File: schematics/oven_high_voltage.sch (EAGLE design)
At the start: 6 parts, among them M1 Convection Fan

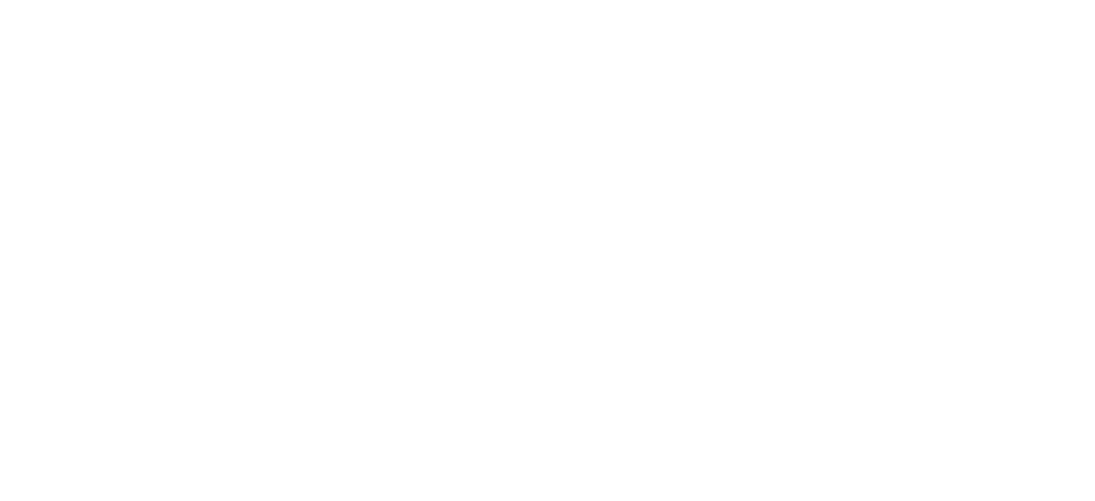
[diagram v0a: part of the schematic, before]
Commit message: Add custom title block.
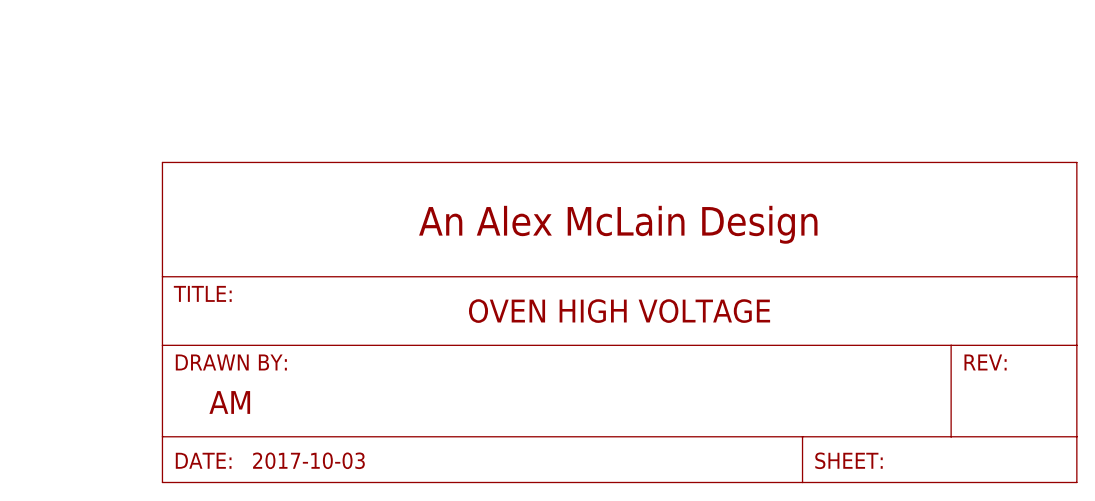
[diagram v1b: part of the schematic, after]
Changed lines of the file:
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@@
 <part name="M1" library="SparkFun-Electromechanical" deviceset="MOTOR" device="10MM" value="Convection Fan"/>
 <part name="GND1" library="SparkFun-PowerSymbols" deviceset="GND2" device="" value="Chassis Ground"/>
+<part name="FRAME1" library="frames" deviceset="LETTER_L" device="">
+<attribute name="COMPANY_NAME" value="An Alex McLain Design"/>
+<attribute name="DATE_DRAWN" value="2017-10-03"/>
+<attribute name="DRAWN_BY" value="AM"/>
+<attribute name="REV" value=""/>
+<attribute name="SHEET_NUM" value=""/>
+<attribute name="TITLE" value="OVEN HIGH VOLTAGE"/>
+</part>
 </parts>
 <sheets>
@@
 <attribute name="VALUE" x="101.6" y="77.724" size="1.778" layer="96" align="top-center"/>
 </instance>
+<instance part="FRAME1" gate="G$1" x="0" y="0">
+<attribute name="COMPANY_NAME" x="0" y="0" size="1.778" layer="96" display="off"/>
+<attribute name="DATE_DRAWN" x="0" y="0" size="1.778" layer="96" display="off"/>
+<attribute name="DRAWN_BY" x="0" y="0" size="1.778" layer="96" display="off"/>
+<attribute name="REV" x="0" y="0" size="1.778" layer="96" display="off"/>
+<attribute name="SHEET_NUM" x="0" y="0" size="1.778" layer="96" display="off"/>
+<attribute name="TITLE" x="0" y="0" size="1.778" layer="96" display="off"/>
+</instance>
+<instance part="FRAME1" gate="G$2" x="147.32" y="0"/>
 </instances>
 <busses>

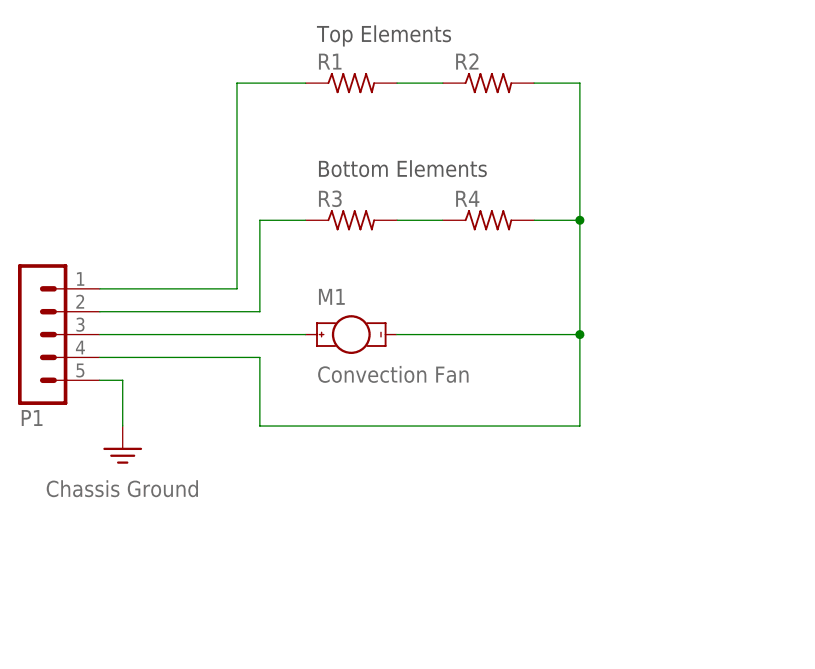
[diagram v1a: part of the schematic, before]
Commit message: Add controller relays schematic.
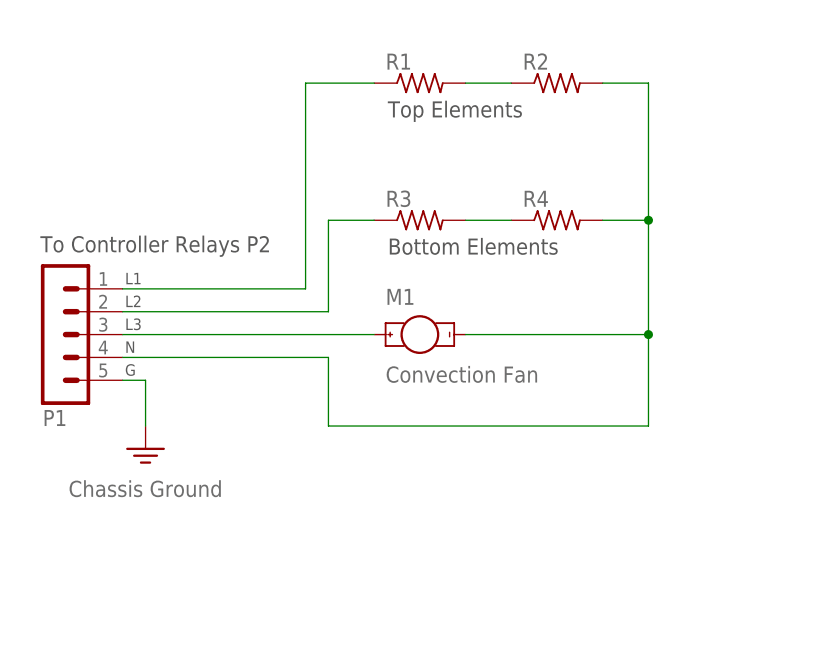
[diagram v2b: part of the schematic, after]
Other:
- note added: "G"
- note added: "L1"
- note added: "L2"
- note added: "L3"
- note added: "N"
- note added: "To Controller Relays P2"
- moved on the sheet: M1, P1, R1, R2, R3, R4
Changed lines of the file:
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@@
 <sheet>
 <plain>
-<text x="123.19" y="126.492" size="1.778" layer="97">Top Elements</text>
-<text x="123.19" y="111.506" size="1.778" layer="97">Bottom Elements</text>
+<text x="131.064" y="118.11" size="1.778" layer="97">Top Elements</text>
+<text x="101.854" y="99.568" size="1.27" layer="97">L1</text>
+<text x="101.854" y="97.028" size="1.27" layer="97">L2</text>
+<text x="101.854" y="94.488" size="1.27" layer="97">L3</text>
+<text x="101.854" y="91.948" size="1.27" layer="97">N</text>
+<text x="101.854" y="89.408" size="1.27" layer="97">G</text>
+<text x="92.456" y="103.124" size="1.778" layer="97">To Controller Relays P2</text>
+<text x="131.064" y="102.87" size="1.778" layer="97">Bottom Elements</text>
 </plain>
 <instances>
-<instance part="R1" gate="G$1" x="127" y="121.92"/>
-<instance part="R2" gate="G$1" x="142.24" y="121.92"/>
-<instance part="R3" gate="G$1" x="127" y="106.68"/>
-<instance part="R4" gate="G$1" x="142.24" y="106.68"/>
-<instance part="P1" gate="G$1" x="91.44" y="93.98" rot="MR180"/>
-<instance part="M1" gate="G$1" x="127" y="93.98" smashed="yes" rot="R90">
-<attribute name="NAME" x="123.19" y="97.282" size="1.778" layer="95" font="vector"/>
-<attribute name="VALUE" x="123.19" y="88.646" size="1.778" layer="96" font="vector"/>
+<instance part="R1" gate="G$1" x="134.62" y="121.92"/>
+<instance part="R2" gate="G$1" x="149.86" y="121.92"/>
+<instance part="R3" gate="G$1" x="134.62" y="106.68"/>
+<instance part="R4" gate="G$1" x="149.86" y="106.68"/>
+<instance part="P1" gate="G$1" x="93.98" y="93.98" rot="MR180"/>
+<instance part="M1" gate="G$1" x="134.62" y="93.98" smashed="yes" rot="R90">
+<attribute name="NAME" x="130.81" y="97.282" size="1.778" layer="95" font="vector"/>
+<attribute name="VALUE" x="130.81" y="88.646" size="1.778" layer="96" font="vector"/>
 </instance>
-<instance part="GND1" gate="G$1" x="101.6" y="81.28" smashed="yes">
-<attribute name="VALUE" x="101.6" y="77.724" size="1.778" layer="96" align="top-center"/>
+<instance part="GND1" gate="G$1" x="104.14" y="81.28" smashed="yes">
+<attribute name="VALUE" x="104.14" y="77.724" size="1.778" layer="96" align="top-center"/>
 </instance>
 <instance part="FRAME1" gate="G$1" x="0" y="0">
@@
 <pinref part="R1" gate="G$1" pin="2"/>
 <pinref part="R2" gate="G$1" pin="1"/>
-<wire x1="132.08" y1="121.92" x2="137.16" y2="121.92" width="0.1524" layer="91"/>
+<wire x1="139.7" y1="121.92" x2="144.78" y2="121.92" width="0.1524" layer="91"/>
 </segment>
 </net>
@@
 <pinref part="R3" gate="G$1" pin="2"/>
 <pinref part="R4" gate="G$1" pin="1"/>
-<wire x1="132.08" y1="106.68" x2="137.16" y2="106.68" width="0.1524" layer="91"/>
+<wire x1="139.7" y1="106.68" x2="144.78" y2="106.68" width="0.1524" layer="91"/>
 </segment>
 </net>
@@
 <pinref part="P1" gate="G$1" pin="3"/>
 <pinref part="M1" gate="G$1" pin="+"/>
-<wire x1="99.06" y1="93.98" x2="121.92" y2="93.98" width="0.1524" layer="91"/>
+<wire x1="101.6" y1="93.98" x2="129.54" y2="93.98" width="0.1524" layer="91"/>
 </segment>
 </net>
@@
 <segment>
 <pinref part="P1" gate="G$1" pin="2"/>
-<wire x1="99.06" y1="96.52" x2="116.84" y2="96.52" width="0.1524" layer="91"/>
-<wire x1="116.84" y1="96.52" x2="116.84" y2="106.68" width="0.1524" layer="91"/>
+<wire x1="101.6" y1="96.52" x2="124.46" y2="96.52" width="0.1524" layer="91"/>
+<wire x1="124.46" y1="96.52" x2="124.46" y2="106.68" width="0.1524" layer="91"/>
 <pinref part="R3" gate="G$1" pin="1"/>
-<wire x1="116.84" y1="106.68" x2="121.92" y2="106.68" width="0.1524" layer="91"/>
+<wire x1="124.46" y1="106.68" x2="129.54" y2="106.68" width="0.1524" layer="91"/>
 </segment>
 </net>
@@
 <segment>
 <pinref part="P1" gate="G$1" pin="1"/>
-<wire x1="99.06" y1="99.06" x2="114.3" y2="99.06" width="0.1524" layer="91"/>
-<wire x1="114.3" y1="99.06" x2="114.3" y2="121.92" width="0.1524" layer="91"/>
+<wire x1="101.6" y1="99.06" x2="121.92" y2="99.06" width="0.1524" layer="91"/>
+<wire x1="121.92" y1="99.06" x2="121.92" y2="121.92" width="0.1524" layer="91"/>
 <pinref part="R1" gate="G$1" pin="1"/>
-<wire x1="114.3" y1="121.92" x2="121.92" y2="121.92" width="0.1524" layer="91"/>
+<wire x1="121.92" y1="121.92" x2="129.54" y2="121.92" width="0.1524" layer="91"/>
 </segment>
 </net>
@@
 <segment>
 <pinref part="M1" gate="G$1" pin="-"/>
-<wire x1="132.08" y1="93.98" x2="152.4" y2="93.98" width="0.1524" layer="91"/>
-<wire x1="152.4" y1="93.98" x2="152.4" y2="83.82" width="0.1524" layer="91"/>
-<wire x1="152.4" y1="83.82" x2="116.84" y2="83.82" width="0.1524" layer="91"/>
-<wire x1="116.84" y1="83.82" x2="116.84" y2="91.44" width="0.1524" layer="91"/>
+<wire x1="139.7" y1="93.98" x2="160.02" y2="93.98" width="0.1524" layer="91"/>
+<wire x1="160.02" y1="93.98" x2="160.02" y2="83.82" width="0.1524" layer="91"/>
+<wire x1="160.02" y1="83.82" x2="124.46" y2="83.82" width="0.1524" layer="91"/>
+<wire x1="124.46" y1="83.82" x2="124.46" y2="91.44" width="0.1524" layer="91"/>
 <pinref part="P1" gate="G$1" pin="4"/>
-<wire x1="116.84" y1="91.44" x2="99.06" y2="91.44" width="0.1524" layer="91"/>
+<wire x1="124.46" y1="91.44" x2="101.6" y2="91.44" width="0.1524" layer="91"/>
 <pinref part="R4" gate="G$1" pin="2"/>
-<wire x1="147.32" y1="106.68" x2="152.4" y2="106.68" width="0.1524" layer="91"/>
-<wire x1="152.4" y1="106.68" x2="152.4" y2="93.98" width="0.1524" layer="91"/>
-<junction x="152.4" y="93.98"/>
+<wire x1="154.94" y1="106.68" x2="160.02" y2="106.68" width="0.1524" layer="91"/>
+<wire x1="160.02" y1="106.68" x2="160.02" y2="93.98" width="0.1524" layer="91"/>
+<junction x="160.02" y="93.98"/>
 <pinref part="R2" gate="G$1" pin="2"/>
-<wire x1="147.32" y1="121.92" x2="152.4" y2="121.92" width="0.1524" layer="91"/>
-<wire x1="152.4" y1="121.92" x2="152.4" y2="106.68" width="0.1524" layer="91"/>
-<junction x="152.4" y="106.68"/>
+<wire x1="154.94" y1="121.92" x2="160.02" y2="121.92" width="0.1524" layer="91"/>
+<wire x1="160.02" y1="121.92" x2="160.02" y2="106.68" width="0.1524" layer="91"/>
+<junction x="160.02" y="106.68"/>
 </segment>
 </net>
@@
 <pinref part="P1" gate="G$1" pin="5"/>
 <pinref part="GND1" gate="G$1" pin="3.3V"/>
-<wire x1="99.06" y1="88.9" x2="101.6" y2="88.9" width="0.1524" layer="91"/>
-<wire x1="101.6" y1="88.9" x2="101.6" y2="83.82" width="0.1524" layer="91"/>
+<wire x1="101.6" y1="88.9" x2="104.14" y2="88.9" width="0.1524" layer="91"/>
+<wire x1="104.14" y1="88.9" x2="104.14" y2="83.82" width="0.1524" layer="91"/>
 </segment>
 </net>
